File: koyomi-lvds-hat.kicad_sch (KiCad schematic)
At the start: 25 parts, among them IC1 SN75LVDS83B, J1 RPi_GPIO, J2 20374-R30E-31, J3 aux_sig, J4 qwiic, J5 Conn_01x06, J6 Conn_01x06, J7 Conn_01x06, U1 AP2114H-2.5

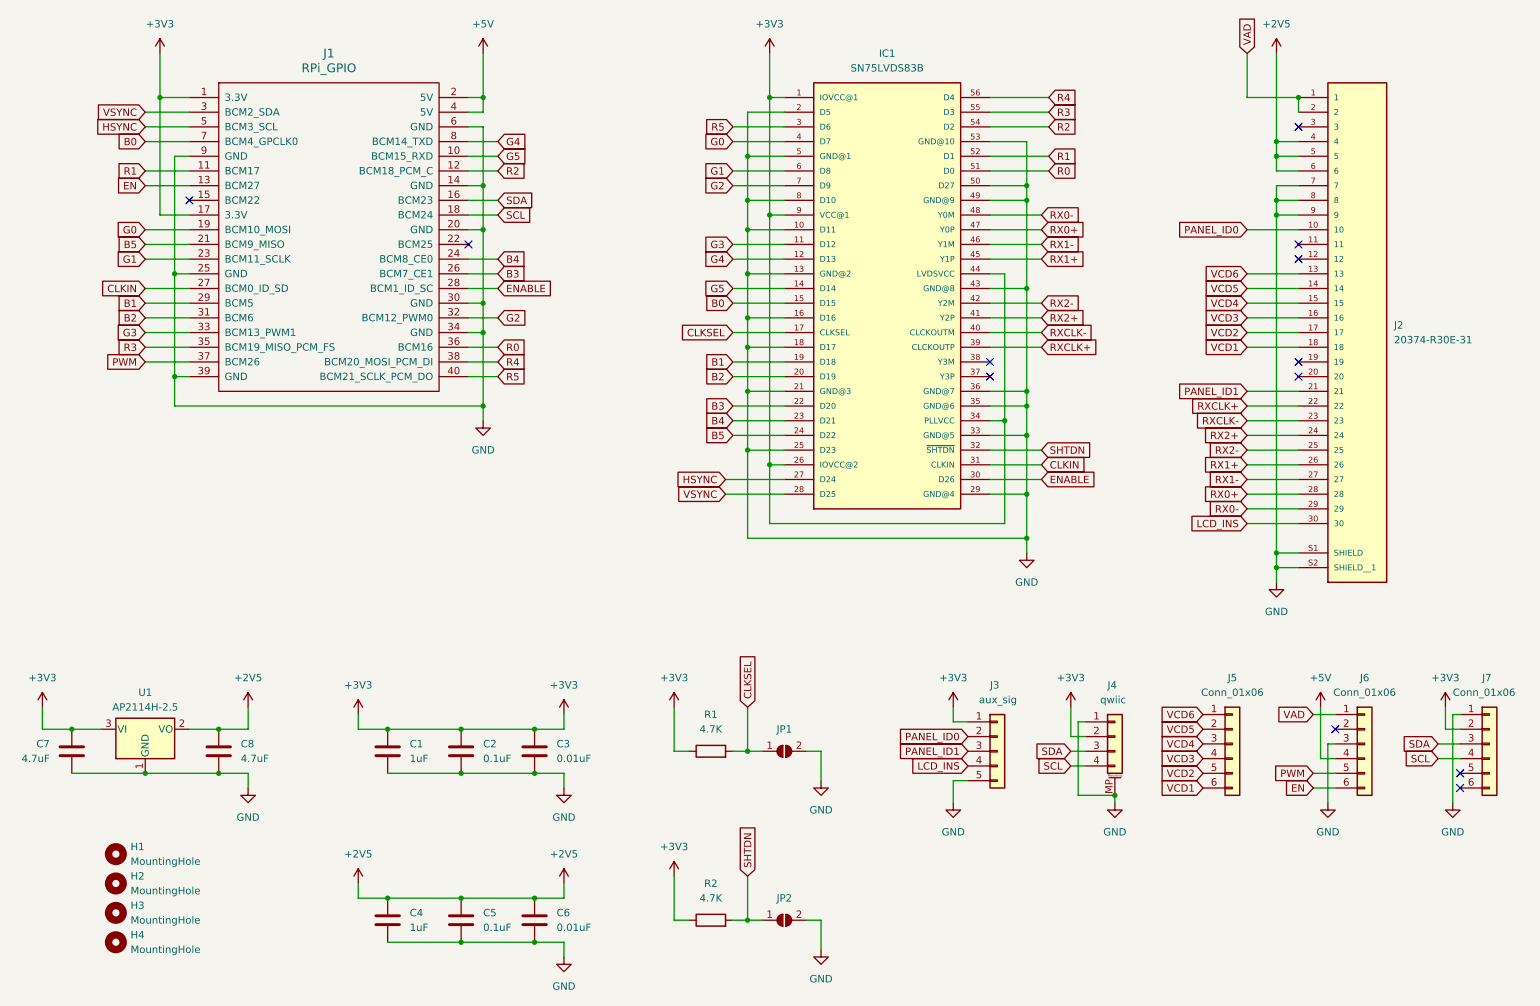
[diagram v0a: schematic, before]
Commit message: RPi/breakout garden standard header with IO22 as INT and IO25 added on top; RGB tracks moved around a bit but length-matched anew
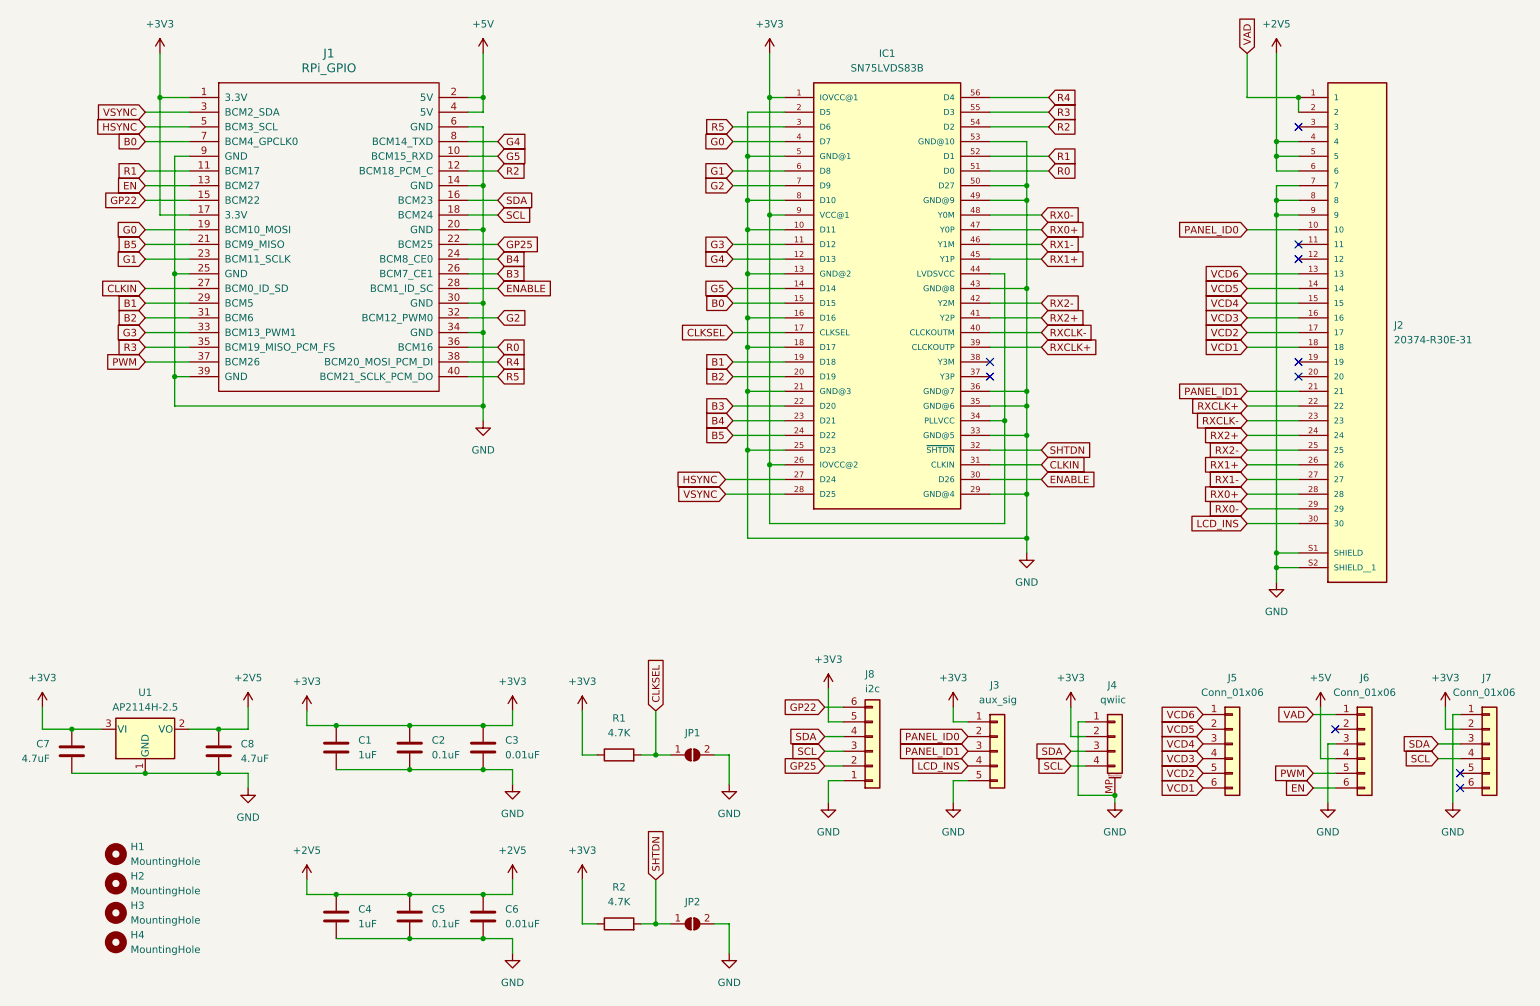
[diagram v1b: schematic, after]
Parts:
- added J8: i2c, Connector_PinSocket_2.54mm:PinSocket_1x06_P2.54mm_Vertical, symbol Connector_Generic:Conn_01x06
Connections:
- net +3V3: now also J8.5 (Pin_5)
- net GND: now also J8.1 (Pin_1)
- net SCL: now also J8.3 (Pin_3)
- net SDA: now also J8.4 (Pin_4)
- net GP22: now reaches J1.15 (BCM22)
- net GP22: now also J8.6 (Pin_6)
- net GP25: now reaches J1.22 (BCM25)
- net GP25: now also J8.2 (Pin_2)
- no-connect marks 12 -> 10
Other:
- moved on the sheet: C1, C2, C3, C4, C5, C6, JP1, JP2, R1, R2

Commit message: v1.1 - fixed hat connector side, added series resistors
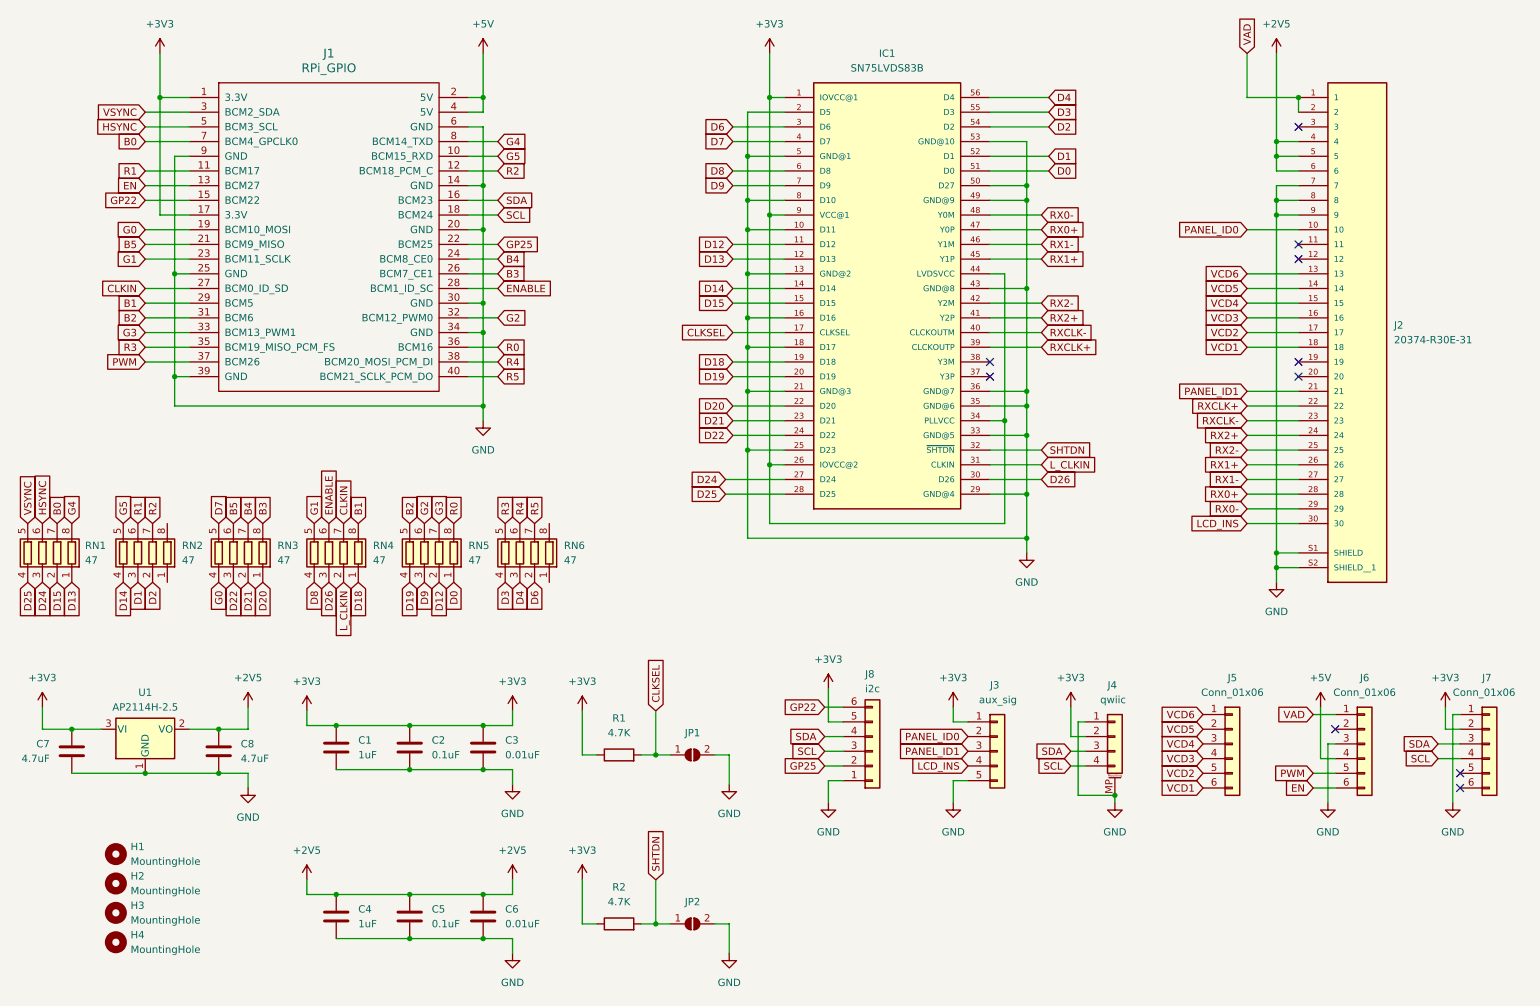
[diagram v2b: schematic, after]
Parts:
- added RN1, RN2, RN3, RN4, RN5, RN6: 47, Resistor_SMD:R_Array_Convex_4x0603, symbol Device:R_Pack04
- C1, C2, C3, C4, C5, C6, C7, C8: footprint PCM_Capacitor_SMD_US_Handsoldering_AKL:C_0603_1608Metric -> Capacitor_SMD:C_0603_1608Metric_Pad1.08x0.95mm_HandSolder
- J8: footprint Connector_PinSocket_2.54mm:PinSocket_1x06_P2.54mm_Vertical -> Connector_PinHeader_2.54mm:PinHeader_1x06_P2.54mm_Vertical
- R1, R2: footprint Capacitor_SMD:C_0603_1608Metric -> Resistor_SMD:R_0603_1608Metric_Pad0.98x0.95mm_HandSolder
- U1: footprint PCM_Package_TO_SOT_SMD_AKL:SOT-223-3_TabPin2 -> Package_TO_SOT_SMD:SOT-223-3_TabPin2
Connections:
- net B0: now also RN1.7 (R2.2); no longer IC1.15 (D15)
- net B1: now also RN4.8 (R1.2); no longer IC1.19 (D18)
- net B2: now also RN5.5 (R4.2); no longer IC1.20 (D19)
- net B3: now also RN3.8 (R1.2); no longer IC1.22 (D20)
- net B4: now also RN3.7 (R2.2); no longer IC1.23 (D21)
- net B5: now also RN3.6 (R3.2); no longer IC1.24 (D22)
- net CLKIN: now also RN4.7 (R2.2); no longer IC1.31 (CLKIN)
- net ENABLE: now also RN4.6 (R3.2); no longer IC1.30 (D26)
- net G0: now also RN3.4 (R4.1); no longer IC1.4 (D7)
- net G1: now also RN4.5 (R4.2); no longer IC1.6 (D8)
- net G2: now also RN5.6 (R3.2); no longer IC1.7 (D9)
- net G3: now also RN5.7 (R2.2); no longer IC1.11 (D12)
- net G4: now also RN1.8 (R1.2); no longer IC1.12 (D13)
- net G5: now also RN2.5 (R4.2); no longer IC1.14 (D14)
- net HSYNC: now also RN1.6 (R3.2); no longer IC1.27 (D24)
- net R0: now also RN5.8 (R1.2); no longer IC1.51 (D0)
- net R1: now also RN2.6 (R3.2); no longer IC1.52 (D1)
- net R2: now also RN2.7 (R2.2); no longer IC1.54 (D2)
- net R3: now also RN6.5 (R4.2); no longer IC1.55 (D3)
- net R4: now also RN6.6 (R3.2); no longer IC1.56 (D4)
- net R5: now also RN6.7 (R2.2); no longer IC1.3 (D6)
- net VSYNC: now also RN1.5 (R4.2); no longer IC1.28 (D25)
- new net D0: IC1.51 (D0), RN5.1 (R1.1)
- new net D1: IC1.52 (D1), RN2.3 (R3.1)
- new net D12: IC1.11 (D12), RN5.2 (R2.1)
- new net D13: IC1.12 (D13), RN1.1 (R1.1)
- new net D14: IC1.14 (D14), RN2.4 (R4.1)
- new net D15: IC1.15 (D15), RN1.2 (R2.1)
- new net D18: IC1.19 (D18), RN4.1 (R1.1)
- new net D19: IC1.20 (D19), RN5.4 (R4.1)
- new net D2: IC1.54 (D2), RN2.2 (R2.1)
- new net D20: IC1.22 (D20), RN3.1 (R1.1)
- new net D21: IC1.23 (D21), RN3.2 (R2.1)
- new net D22: IC1.24 (D22), RN3.3 (R3.1)
- new net D24: IC1.27 (D24), RN1.3 (R3.1)
- new net D25: IC1.28 (D25), RN1.4 (R4.1)
- new net D26: IC1.30 (D26), RN4.3 (R3.1)
- new net D3: IC1.55 (D3), RN6.4 (R4.1)
- new net D4: IC1.56 (D4), RN6.3 (R3.1)
- new net D6: IC1.3 (D6), RN6.2 (R2.1)
- new net D7: IC1.4 (D7), RN3.5 (R4.2)
- new net D8: IC1.6 (D8), RN4.4 (R4.1)
- new net D9: IC1.7 (D9), RN5.3 (R3.1)
- new net L_CLKIN: IC1.31 (CLKIN), RN4.2 (R2.1)

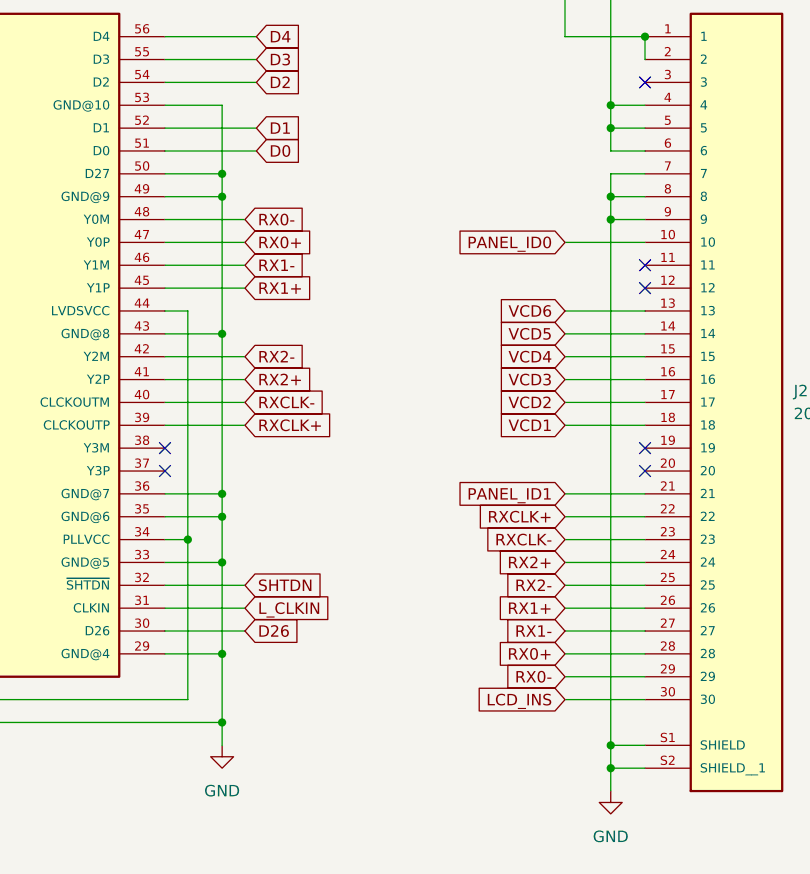
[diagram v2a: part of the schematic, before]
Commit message: Added LVDS common mode filters
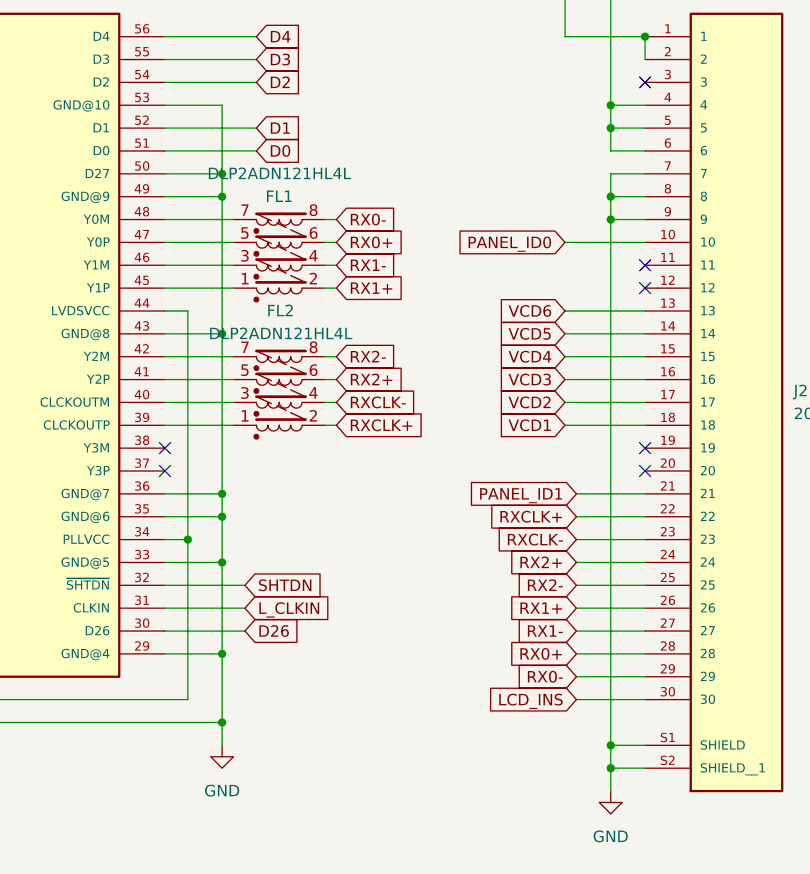
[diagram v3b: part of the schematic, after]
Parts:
- added FL1, FL2: DLP2ADN121HL4L, Murata_DLP2ADN121HL4L:Murata_DLP2ADN121HL4L, symbol Device:Filter_EMI_LLLL
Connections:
- net RX0+: now also FL1.6; no longer IC1.47 (Y0P)
- net RX0-: now also FL1.8; no longer IC1.48 (Y0M)
- net RX1+: now also FL1.2; no longer IC1.45 (Y1P)
- net RX1-: now also FL1.4; no longer IC1.46 (Y1M)
- net RX2+: now also FL2.6; no longer IC1.41 (Y2P)
- net RX2-: now also FL2.8; no longer IC1.42 (Y2M)
- net RXCLK+: now also FL2.2; no longer IC1.39 (CLCKOUTP)
- net RXCLK-: now also FL2.4; no longer IC1.40 (CLCKOUTM)
- new net: FL2.1, IC1.39 (CLCKOUTP)
- new net: FL2.3, IC1.40 (CLCKOUTM)
- new net: FL2.5, IC1.41 (Y2P)
- new net: FL2.7, IC1.42 (Y2M)
- new net: FL1.1, IC1.45 (Y1P)
- new net: FL1.3, IC1.46 (Y1M)
- new net: FL1.5, IC1.47 (Y0P)
- new net: FL1.7, IC1.48 (Y0M)

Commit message: Gerbers and JLCPCB files update
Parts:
- C2, C5: value 0.1uF -> 100nF
- C3, C6: value 0.01uF -> 10nF
- FL1: now in the parts list
- H1, H2, H3, H4, J3, J5, J6, J7, J8, JP1, JP2: now left out of the parts list
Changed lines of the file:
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@@
 		(unit 1)
 		(exclude_from_sim no)
-		(in_bom yes)
+		(in_bom no)
 		(on_board yes)
 		(dnp no)
@@
 		(unit 1)
 		(exclude_from_sim no)
-		(in_bom yes)
+		(in_bom no)
 		(on_board yes)
 		(dnp no)
@@
 			)
 		)
-		(property "Value" "0.01uF"
+		(property "Value" "10nF"
 			(at 101.6 144.145 0)
 			(effects
@@
 		(unit 1)
 		(exclude_from_sim no)
-		(in_bom yes)
+		(in_bom no)
 		(on_board yes)
 		(dnp no)
@@
 		(unit 1)
 		(exclude_from_sim no)
-		(in_bom yes)
+		(in_bom no)
 		(on_board yes)
 		(dnp no)
@@
 		(unit 1)
 		(exclude_from_sim no)
-		(in_bom yes)
+		(in_bom no)
 		(on_board yes)
 		(dnp no)
@@
 		(unit 1)
 		(exclude_from_sim no)
-		(in_bom no)
+		(in_bom yes)
 		(on_board yes)
 		(dnp no)
@@
 		(unit 1)
 		(exclude_from_sim no)
-		(in_bom yes)
+		(in_bom no)
 		(on_board yes)
 		(dnp no)
@@
 		(unit 1)
 		(exclude_from_sim no)
-		(in_bom yes)
+		(in_bom no)
 		(on_board yes)
 		(dnp no)
@@
 			)
 		)
-		(property "Value" "0.1uF"
+		(property "Value" "100nF"
 			(at 88.9 173.355 0)
 			(effects
@@
 		(unit 1)
 		(exclude_from_sim no)
-		(in_bom yes)
+		(in_bom no)
 		(on_board yes)
 		(dnp no)
@@
 		(unit 1)
 		(exclude_from_sim no)
-		(in_bom yes)
+		(in_bom no)
 		(on_board yes)
 		(dnp no)
@@
 			)
 		)
-		(property "Value" "0.01uF"
+		(property "Value" "10nF"
 			(at 101.6 173.355 0)
 			(effects
@@
 			)
 		)
-		(property "Value" "0.1uF"
+		(property "Value" "100nF"
 			(at 88.9 144.145 0)
 			(effects
@@
 		(unit 1)
 		(exclude_from_sim no)
-		(in_bom yes)
+		(in_bom no)
 		(on_board yes)
 		(dnp no)
@@
 		(unit 1)
 		(exclude_from_sim no)
-		(in_bom yes)
+		(in_bom no)
 		(on_board yes)
 		(dnp no)
